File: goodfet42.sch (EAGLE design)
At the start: 11 parts, among them U1 MSP430F2618TPM, U2 FT232RL

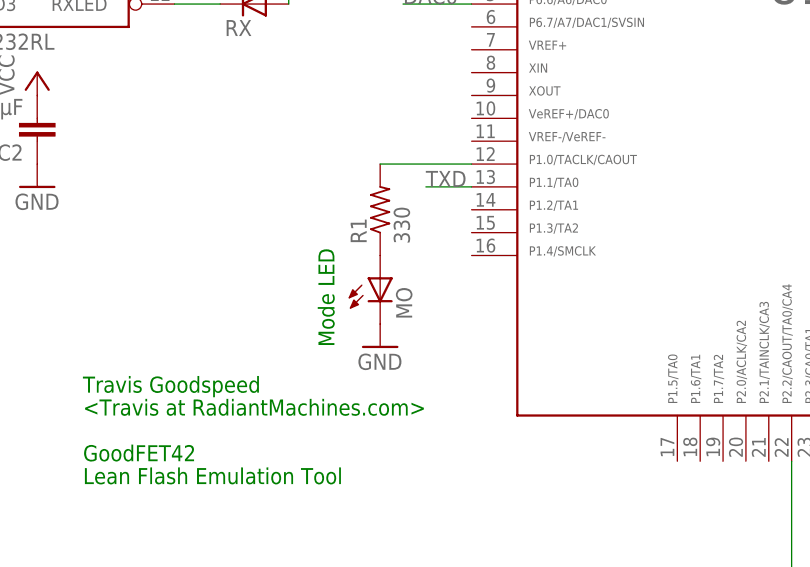
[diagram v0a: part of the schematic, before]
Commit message: rename MO LED to MODE, silkscreen fixes, add Homebrew PCB designation
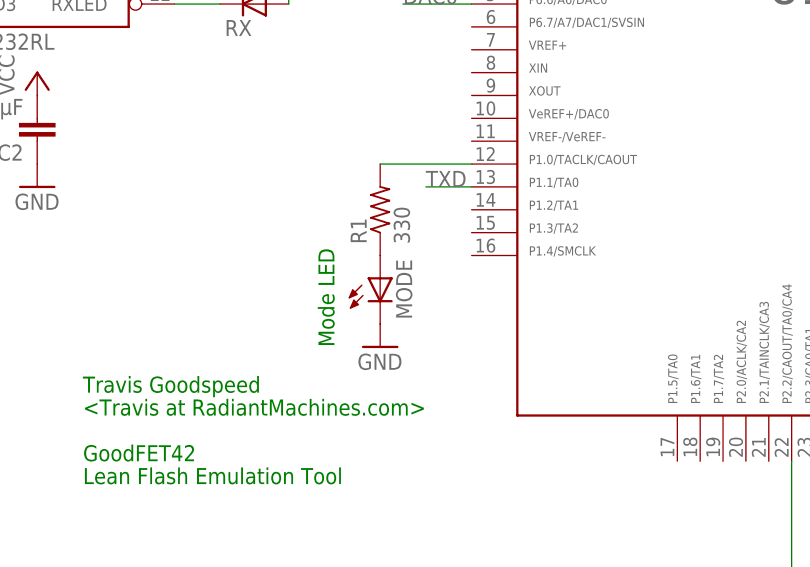
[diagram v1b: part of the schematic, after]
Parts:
- renumbered MO to MODE
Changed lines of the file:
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@@
 <part name="C1" library="rcl" deviceset="C-EU" device="C0603" value="0.1µF"/>
 <part name="R1" library="rcl" deviceset="R-US_" device="R0603" value="330"/>
-<part name="MO" library="led" deviceset="LED" device="CHIP-LED0603"/>
+<part name="MODE" library="led" deviceset="LED" device="CHIP-LED0603"/>
 <part name="GND1" library="supply1" deviceset="GND" device=""/>
 <part name="U2" library="SparkFun" deviceset="FT232RL-BASIC" device="SSOP" value="FT232RL"/>
@@
 <instance part="C1" gate="G$1" x="55.88" y="101.6" rot="R270"/>
 <instance part="R1" gate="G$1" x="33.02" y="35.56" rot="R90"/>
-<instance part="MO" gate="G$1" x="33.02" y="27.94"/>
+<instance part="MODE" gate="G$1" x="33.02" y="27.94"/>
 <instance part="GND1" gate="1" x="33.02" y="20.32"/>
 <instance part="U2" gate="G$1" x="-5.08" y="73.66"/>
@@
 </segment>
 <segment>
-<pinref part="MO" gate="G$1" pin="C"/>
+<pinref part="MODE" gate="G$1" pin="C"/>
 <pinref part="GND1" gate="1" pin="GND"/>
 </segment>
@@
 <segment>
 <pinref part="R1" gate="G$1" pin="1"/>
-<pinref part="MO" gate="G$1" pin="A"/>
-</segment>
-</net>
+<pinref part="MODE" gate="G$1" pin="A"/>
+</segment>
+</net>
